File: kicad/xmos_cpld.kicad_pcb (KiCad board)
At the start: 2 copper layers, 48 x 24.8 mm, 14 parts, among them P1 CONN_02X05, U1 5M40ZE64, U2 NCP699SN18

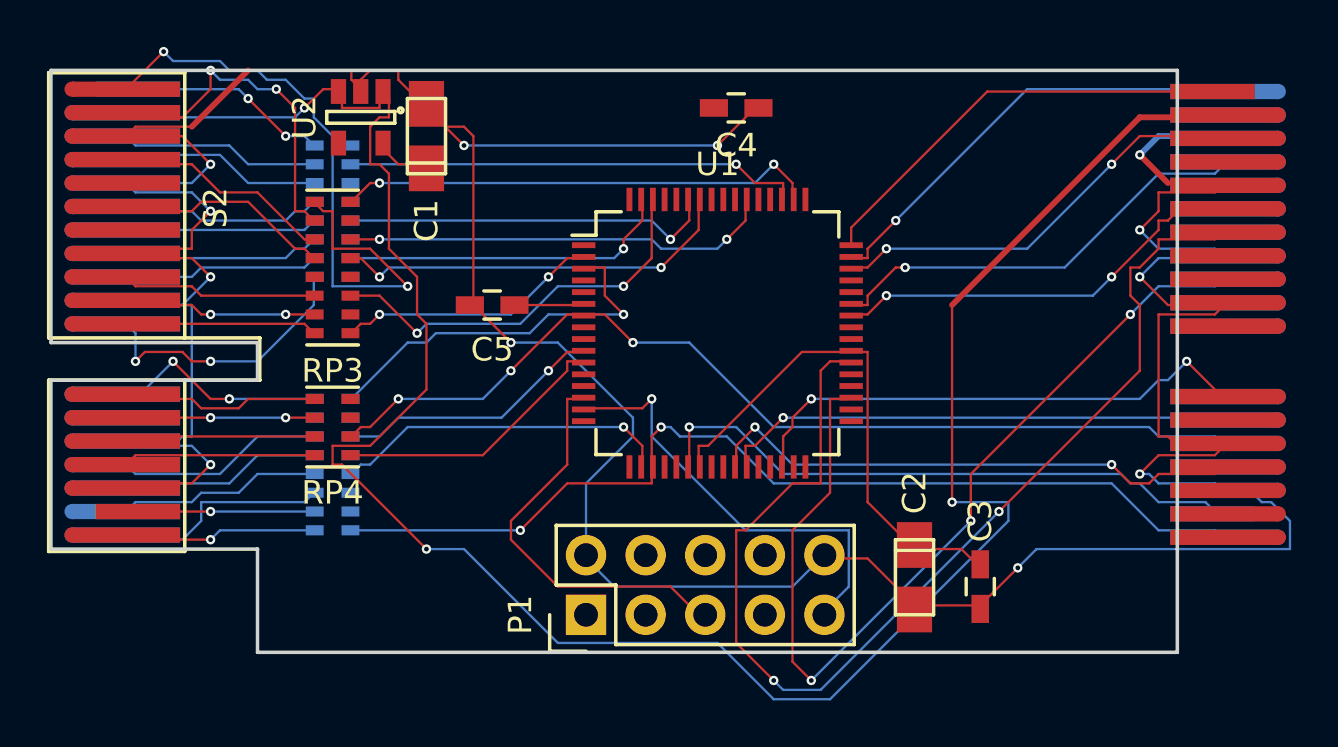
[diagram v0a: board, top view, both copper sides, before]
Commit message: 1V8 pwr chip goes to other edge of the board. GND zones added.
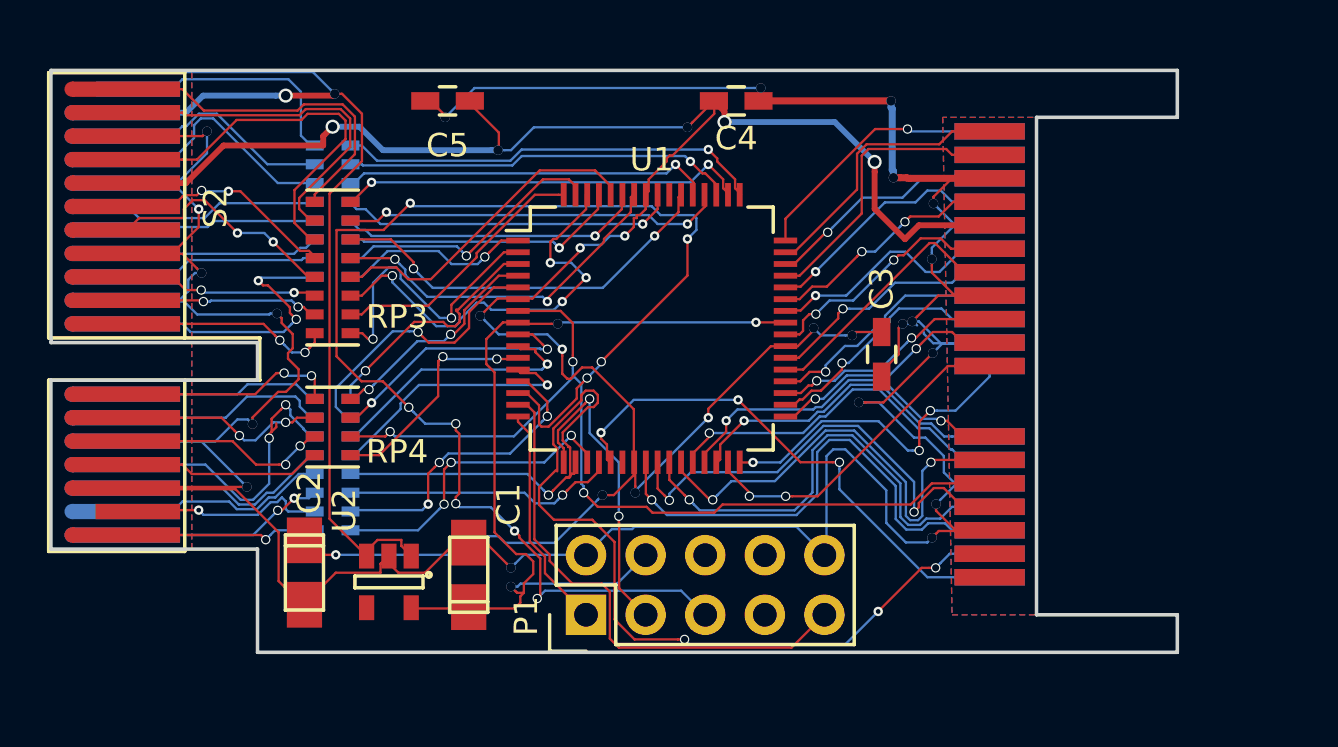
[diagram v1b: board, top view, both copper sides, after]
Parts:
- RP1, RP2, RP3: value R_PACK8 -> 33R
- RP4: value R_PACK4 -> 33R
- S1: footprint Connect:PCI-EXPRESS -> m:PCIe_36
- moved C2 26.0 mm to (70.8, 81.4)
- moved U2 19.8 mm to (74.4, 81.8)
- moved C1 18.8 mm to (77.8, 81.5)
- moved S1 15.0 mm to (100.0, 81.6)
- moved C3 10.8 mm to (95.4, 72.1)
- moved C5 8.91 mm to (76.9, 61.3)
- moved U1 2.81 mm to (85.6, 71.0)
- moved C4 0.30 mm to (89.2, 61.3)
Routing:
- net +3V3: track 26.0 -> 105.0 mm, vias 0 -> 15
- net +5V: track 97.1 -> 44.7 mm, vias 3 -> 2
- net /F1TMS: track 17.5 -> 59.2 mm, vias 0 -> 9
- net /BA7: track 48.7 -> 10.3 mm, vias 2 -> 1
- net +1V8: track 2.69 -> 37.7 mm, vias 0 -> 3
- net /~ARST: track 14.5 -> 47.0 mm, vias 1 -> 4
- net /BB9: track 39.9 -> 10.0 mm, vias 3 -> 2
- net /AB18: track 42.5 -> 13.4 mm, vias 2 -> 3
- net /BB17: track 25.7 -> 0.00 mm, vias 1 -> 0
- net /BA18: track 0.00 -> 22.4 mm, vias 0 -> 3
- net /BA16: track 0.00 -> 21.4 mm, vias 0 -> 1
- net /BB15: track 0.00 -> 20.1 mm, vias 0 -> 2
- net /AA1: track 0.00 -> 18.3 mm, vias 0 -> 1
- net /AB2: track 0.00 -> 16.4 mm, vias 0 -> 2
- net /AA4: track 0.00 -> 15.8 mm, vias 0 -> 1
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- added copper zone on B.Cu, net GND
- added copper zone on F.Cu, net GND
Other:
- outline, holes or cut-outs redrawn
- net class Default: clearance 0.1 -> 0.2; trace_width 0.1 -> 0.25; via_dia 0.4 -> 0.6; via_drill 0.3 -> 0.4
- net class Ground added: clearance 0.3, trace_width 0.3, via_dia 0.6, via_drill 0.4
- net class Signal added: clearance 0.1, trace_width 0.1, via_dia 0.4, via_drill 0.3
- rule pad_to_mask_clearance: 0.2 -> 0.1
- rule trace_clearance: 0.1 -> 0.2

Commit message: add p55, gnd.
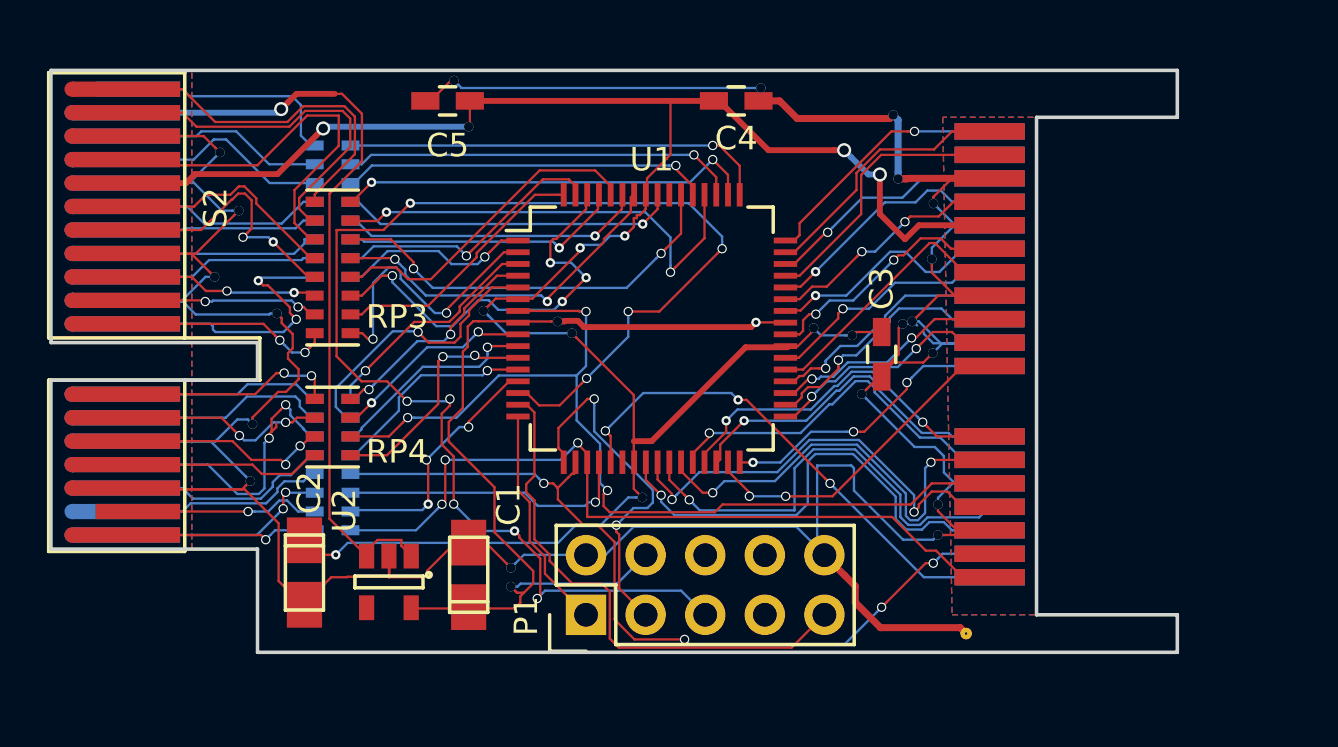
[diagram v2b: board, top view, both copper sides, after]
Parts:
- added P16: Pillar, confjmpblock:Pillar, F.Cu at (99.0, 84.0)
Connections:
- S1 pad B18: /AB18 -> /BB18
- U1 pad 20: /AA18 -> /BB18
- U1 pad 55: (no net) -> /AA18
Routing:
- net /AB18: track 13.4 -> 31.0 mm
- net GND: track 182.3 -> 194.2 mm
- net /~ARST: track 47.0 -> 35.6 mm
- net +5V: track 44.7 -> 33.7 mm, vias 2 -> 1
- net +3V3: track 105.0 -> 100.1 mm, vias 15 -> 12
- net /BB18: track 0.00 -> 4.80 mm, vias 0 -> 1
- net /AB2: track 16.4 -> 19.6 mm
- net /AB13: track 11.1 -> 8.70 mm
- net /AA16: track 11.3 -> 8.98 mm
- net /AA15: track 11.3 -> 9.05 mm
- net /AB17: track 13.1 -> 10.8 mm
- net +1V8: track 37.7 -> 39.8 mm
- net /BA11: track 14.4 -> 12.5 mm
- net /F1TDO: track 13.5 -> 15.3 mm
- net Net-(RP3-Pad5): track 10.2 -> 11.7 mm
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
